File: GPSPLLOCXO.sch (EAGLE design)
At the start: 26 parts, among them IC1 74AC14D, IC2 74LS86D, IC3 74LS390D, IC4 74LS390D, X1 5566-10

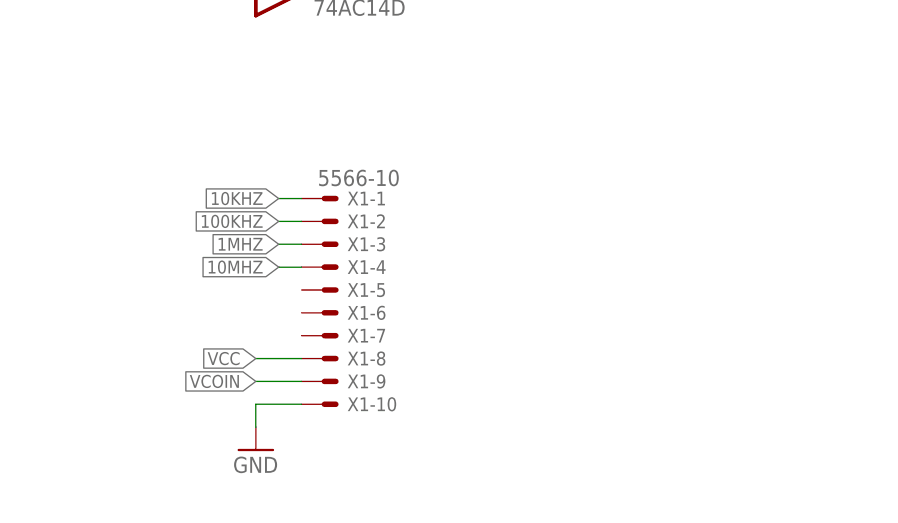
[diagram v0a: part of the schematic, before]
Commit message: Modified board to suite CNC/Milling
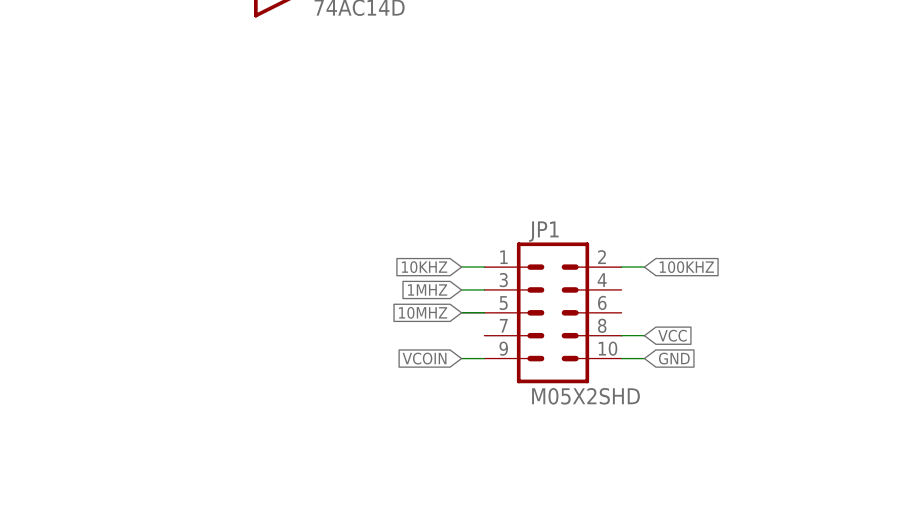
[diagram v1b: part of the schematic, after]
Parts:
- removed X1: 5566-10, con-molex:5566-10
- added JP1: M05X2SHD, SparkFun-Connectors:M05X2SHD
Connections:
- net 100KHZ: now also JP1.2; no longer X1-2.S
- net 10KHZ: now also JP1.1; no longer X1-1.S
- net 10MHZ: now also JP1.5; no longer X1-4.S
- net 1MHZ: now also JP1.3; no longer X1-3.S
- net GND: now also JP1.10; no longer X1-10.S
- net VCC: now also JP1.8; no longer X1-8.S
- net VCOIN: now also JP1.9; no longer X1-9.S
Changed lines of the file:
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@@
 <layer number="54" name="bGND_GNDA" color="1" fill="9" visible="no" active="no"/>
 <layer number="56" name="wert" color="7" fill="1" visible="no" active="no"/>
+<layer number="57" name="tCAD" color="7" fill="1" visible="no" active="no"/>
 <layer number="91" name="Nets" color="2" fill="1" visible="yes" active="yes"/>
 <layer number="92" name="Busses" color="1" fill="1" visible="yes" active="yes"/>
@@
 <layer number="97" name="Info" color="7" fill="1" visible="yes" active="yes"/>
 <layer number="98" name="Guide" color="6" fill="1" visible="yes" active="yes"/>
+<layer number="99" name="SpiceOrder" color="7" fill="1" visible="yes" active="yes"/>
 <layer number="100" name="Muster" color="7" fill="1" visible="no" active="no"/>
 <layer number="101" name="Patch_Top" color="12" fill="4" visible="yes" active="yes"/>
@@
 <layer number="108" name="tplace-old" color="10" fill="1" visible="yes" active="yes"/>
 <layer number="109" name="ref-old" color="11" fill="1" visible="yes" active="yes"/>
+<layer number="110" name="fp0" color="7" fill="1" visible="yes" active="yes"/>
+<layer number="111" name="LPC17xx" color="7" fill="1" visible="yes" active="yes"/>
+<layer number="112" name="tSilk" color="7" fill="1" visible="yes" active="yes"/>
+<layer number="113" name="IDFDebug" color="4" fill="1" visible="yes" active="yes"/>
 <layer number="116" name="Patch_BOT" color="9" fill="4" visible="yes" active="yes"/>
 <layer number="121" name="_tsilk" color="7" fill="1" visible="yes" active="yes"/>
 <layer number="122" name="_bsilk" color="7" fill="1" visible="yes" active="yes"/>
+<layer number="123" name="tTestmark" color="7" fill="1" visible="yes" active="yes"/>
+<layer number="124" name="bTestmark" color="7" fill="1" visible="yes" active="yes"/>
 <layer number="125" name="_tNames" color="7" fill="1" visible="yes" active="yes"/>
+<layer number="126" name="_bNames" color="7" fill="1" visible="yes" active="yes"/>
+<layer number="127" name="_tValues" color="7" fill="1" visible="yes" active="yes"/>
+<layer number="128" name="_bValues" color="7" fill="1" visible="yes" active="yes"/>
+<layer number="131" name="tAdjust" color="7" fill="1" visible="yes" active="yes"/>
+<layer number="132" name="bAdjust" color="7" fill="1" visible="yes" active="yes"/>
 <layer number="144" name="Drill_legend" color="7" fill="1" visible="yes" active="yes"/>
+<layer number="150" name="Notes" color="7" fill="1" visible="yes" active="yes"/>
 <layer number="151" name="HeatSink" color="7" fill="1" visible="yes" active="yes"/>
+<layer number="152" name="_bDocu" color="7" fill="1" visible="yes" active="yes"/>
+<layer number="153" name="FabDoc1" color="7" fill="1" visible="yes" active="yes"/>
+<layer number="154" name="FabDoc2" color="7" fill="1" visible="yes" active="yes"/>
+<layer number="155" name="FabDoc3" color="7" fill="1" visible="yes" active="yes"/>
 <layer number="199" name="Contour" color="7" fill="1" visible="yes" active="yes"/>
 <layer number="200" name="200bmp" color="1" fill="10" visible="yes" active="yes"/>
@@
 <layer number="223" name="223bmp" color="24" fill="1" visible="no" active="no"/>
 <layer number="224" name="224bmp" color="25" fill="1" visible="no" active="no"/>
+<layer number="248" name="Housing" color="7" fill="1" visible="yes" active="yes"/>
+<layer number="249" name="Edge" color="7" fill="1" visible="yes" active="yes"/>
 <layer number="250" name="Descript" color="3" fill="1" visible="no" active="no"/>
 <layer number="251" name="SMDround" color="12" fill="11" visible="no" active="no"/>
@@
 <part name="GND12" library="supply1" deviceset="GND" device=""/>
 <part name="ISOTEMP131-1" library="untitled" deviceset="ISOTEMP-131-191" device=""/>
-<part name="X1" library="con-molex" deviceset="5566-10" device=""/>
-<part name="GND10" library="supply1" deviceset="GND" device=""/>
+<part name="JP1" library="SparkFun-Connectors" deviceset="M05X2" device="SHD"/>
 </parts>
 <sheets>
@@
 <instance part="GND12" gate="1" x="-78.74" y="-17.78"/>
 <instance part="ISOTEMP131-1" gate="ISOTEMP131-191" x="58.42" y="55.88"/>
-<instance part="X1" gate="-1" x="139.7" y="12.7"/>
-<instance part="X1" gate="-2" x="139.7" y="10.16"/>
-<instance part="X1" gate="-3" x="139.7" y="7.62"/>
-<instance part="X1" gate="-4" x="139.7" y="5.08"/>
-<instance part="X1" gate="-5" x="139.7" y="2.54"/>
-<instance part="X1" gate="-6" x="139.7" y="0"/>
-<instance part="X1" gate="-7" x="139.7" y="-2.54"/>
-<instance part="X1" gate="-8" x="139.7" y="-5.08"/>
-<instance part="X1" gate="-9" x="139.7" y="-7.62"/>
-<instance part="X1" gate="-10" x="139.7" y="-10.16"/>
-<instance part="GND10" gate="1" x="132.08" y="-15.24"/>
+<instance part="JP1" gate="G$1" x="165.1" y="0"/>
 </instances>
 <busses>
@@
 </segment>
 <segment>
-<pinref part="X1" gate="-10" pin="S"/>
-<wire x1="137.16" y1="-10.16" x2="132.08" y2="-10.16" width="0.1524" layer="91"/>
-<wire x1="132.08" y1="-10.16" x2="132.08" y2="-12.7" width="0.1524" layer="91"/>
-<pinref part="GND10" gate="1" pin="GND"/>
+<pinref part="JP1" gate="G$1" pin="10"/>
+<wire x1="172.72" y1="-5.08" x2="175.26" y2="-5.08" width="0.1524" layer="91"/>
+<label x="175.26" y="-5.08" size="1.27" layer="95" xref="yes"/>
 </segment>
 </net>
@@
 </segment>
 <segment>
-<pinref part="X1" gate="-8" pin="S"/>
-<wire x1="137.16" y1="-5.08" x2="132.08" y2="-5.08" width="0.1524" layer="91"/>
-<label x="132.08" y="-5.08" size="1.4224" layer="95" rot="R180" xref="yes"/>
+<pinref part="JP1" gate="G$1" pin="8"/>
+<wire x1="172.72" y1="-2.54" x2="175.26" y2="-2.54" width="0.1524" layer="91"/>
+<label x="175.26" y="-2.54" size="1.27" layer="95" xref="yes"/>
 </segment>
 </net>
@@
 </segment>
 <segment>
-<pinref part="X1" gate="-1" pin="S"/>
-<wire x1="137.16" y1="12.7" x2="134.62" y2="12.7" width="0.1524" layer="91"/>
-<label x="134.62" y="12.7" size="1.4224" layer="95" rot="R180" xref="yes"/>
+<pinref part="JP1" gate="G$1" pin="1"/>
+<wire x1="157.48" y1="5.08" x2="154.94" y2="5.08" width="0.1524" layer="91"/>
+<label x="154.94" y="5.08" size="1.27" layer="95" rot="R180" xref="yes"/>
 </segment>
 </net>
@@
 </segment>
 <segment>
-<pinref part="X1" gate="-3" pin="S"/>
-<wire x1="137.16" y1="7.62" x2="134.62" y2="7.62" width="0.1524" layer="91"/>
-<label x="134.62" y="7.62" size="1.4224" layer="95" rot="R180" xref="yes"/>
+<pinref part="JP1" gate="G$1" pin="3"/>
+<wire x1="157.48" y1="2.54" x2="154.94" y2="2.54" width="0.1524" layer="91"/>
+<label x="154.94" y="2.54" size="1.27" layer="95" rot="R180" xref="yes"/>
 </segment>
 </net>
@@
 </segment>
 <segment>
-<pinref part="X1" gate="-2" pin="S"/>
-<wire x1="137.16" y1="10.16" x2="134.62" y2="10.16" width="0.1524" layer="91"/>
-<label x="134.62" y="10.16" size="1.4224" layer="95" rot="R180" xref="yes"/>
+<pinref part="JP1" gate="G$1" pin="2"/>
+<wire x1="172.72" y1="5.08" x2="175.26" y2="5.08" width="0.1524" layer="91"/>
+<label x="175.26" y="5.08" size="1.27" layer="95" xref="yes"/>
 </segment>
 </net>
@@
 </segment>
 <segment>
-<pinref part="X1" gate="-4" pin="S"/>
-<wire x1="137.16" y1="5.08" x2="134.62" y2="5.08" width="0.1524" layer="91"/>
-<label x="134.62" y="5.08" size="1.4224" layer="95" rot="R180" xref="yes"/>
+<pinref part="JP1" gate="G$1" pin="5"/>
+<wire x1="157.48" y1="0" x2="154.94" y2="0" width="0.1524" layer="91"/>
+<label x="154.94" y="0" size="1.27" layer="95" rot="R180" xref="yes"/>
 </segment>
 </net>
@@
 </segment>
 <segment>
-<pinref part="X1" gate="-9" pin="S"/>
-<wire x1="137.16" y1="-7.62" x2="132.08" y2="-7.62" width="0.1524" layer="91"/>
-<label x="132.08" y="-7.62" size="1.4224" layer="95" rot="R180" xref="yes"/>
-</segment>
-</net>
+<pinref part="JP1" gate="G$1" pin="9"/>
+<wire x1="157.48" y1="-5.08" x2="154.94" y2="-5.08" width="0.1524" layer="91"/>
+<label x="154.94" y="-5.08" size="1.27" layer="95" rot="R180" xref="yes"/>
+</segment>
+</net>

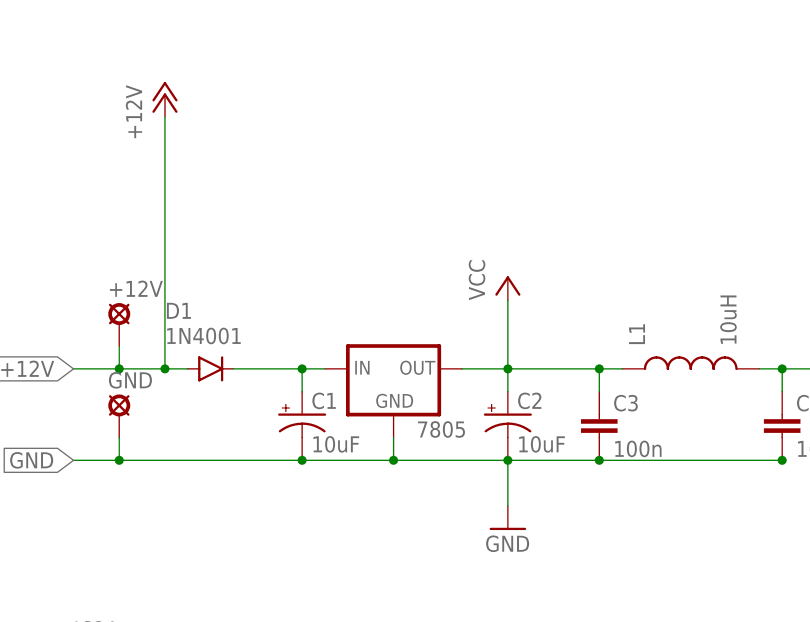
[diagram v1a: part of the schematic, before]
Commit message: Corrected FTDI mapping, added header to select power source.
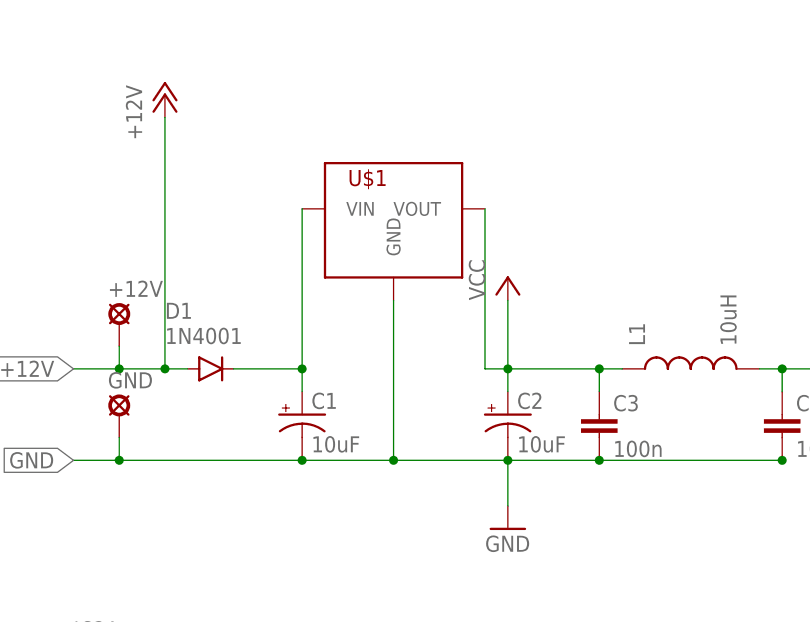
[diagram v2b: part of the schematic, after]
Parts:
- removed 7805: (no value), SparkFun-PowerIC:V_REG_78XXSINK
- added U$1: R-78HBXX-0.5R-78XX-0.5-SIP3, recom:R-78HBXX-0.5R-78XX-0.5-SIP3
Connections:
- net GND: now also U$1.GND; no longer 7805.GND
- net N$1: now also U$1.VIN; no longer 7805.IN
- net VCC: now also U$1.VOUT; no longer 7805.OUT
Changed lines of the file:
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@@
 </classes>
 <parts>
-<part name="7805" library="SparkFun-PowerIC" deviceset="V_REG_78XX" device="SINK"/>
 <part name="D1" library="SparkFun-DiscreteSemi" deviceset="DIODE" device="SMA" value="1N4001"/>
 <part name="C1" library="SparkFun-Capacitors" deviceset="10UF-16V-10%(TANT)" device="" value="10uF"/>
@@
 <part name="ISOTEMP131-1" library="untitled" deviceset="ISOTEMP-131-191" device=""/>
 <part name="JP1" library="SparkFun-Connectors" deviceset="M05X2" device="SHD"/>
+<part name="U$1" library="recom" deviceset="R-78HBXX-0.5" device="R-78XX-0.5-SIP3"/>
 </parts>
 <sheets>
@@
 </plain>
 <instances>
-<instance part="7805" gate="G$1" x="5.08" y="91.44"/>
 <instance part="D1" gate="G$1" x="-15.24" y="91.44" smashed="yes">
 <attribute name="NAME" x="-20.32" y="97.0026" size="1.778" layer="95"/>
@@
 <instance part="ISOTEMP131-1" gate="ISOTEMP131-191" x="58.42" y="55.88"/>
 <instance part="JP1" gate="G$1" x="165.1" y="0"/>
+<instance part="U$1" gate="G$1" x="5.08" y="106.68"/>
 </instances>
 <busses>
@@
 <wire x1="-5.08" y1="81.28" x2="5.08" y2="81.28" width="0.1524" layer="91"/>
 <wire x1="5.08" y1="81.28" x2="17.78" y2="81.28" width="0.1524" layer="91"/>
-<pinref part="7805" gate="G$1" pin="GND"/>
-<wire x1="5.08" y1="81.28" x2="5.08" y2="83.82" width="0.1524" layer="91"/>
 <label x="-30.48" y="81.28" size="1.778" layer="95" rot="R180" xref="yes"/>
 <pinref part="C1" gate="G$1" pin="-"/>
@@
 <pinref part="GND" gate="1" pin="MP"/>
 <wire x1="-25.4" y1="81.28" x2="-25.4" y2="83.82" width="0.1524" layer="91"/>
+<pinref part="U$1" gate="G$1" pin="GND"/>
+<wire x1="5.08" y1="81.28" x2="5.08" y2="99.06" width="0.1524" layer="91"/>
 </segment>
 <segment>
@@
 <net name="VCC" class="0">
 <segment>
-<pinref part="7805" gate="G$1" pin="OUT"/>
-<wire x1="12.7" y1="91.44" x2="17.78" y2="91.44" width="0.1524" layer="91"/>
 <pinref part="C2" gate="G$1" pin="+"/>
 <wire x1="17.78" y1="88.9" x2="17.78" y2="91.44" width="0.1524" layer="91"/>
@@
 <junction x="27.94" y="91.44"/>
 <pinref part="L1" gate="G$1" pin="1"/>
+<wire x1="17.78" y1="91.44" x2="15.24" y2="91.44" width="0.1524" layer="91"/>
+<pinref part="U$1" gate="G$1" pin="VOUT"/>
+<wire x1="15.24" y1="91.44" x2="15.24" y2="109.22" width="0.1524" layer="91"/>
 </segment>
 <segment>
@@
 <segment>
 <pinref part="D1" gate="G$1" pin="C"/>
-<pinref part="7805" gate="G$1" pin="IN"/>
 <wire x1="-12.7" y1="91.44" x2="-5.08" y2="91.44" width="0.1524" layer="91"/>
 <pinref part="C1" gate="G$1" pin="+"/>
-<wire x1="-5.08" y1="91.44" x2="-2.54" y2="91.44" width="0.1524" layer="91"/>
 <wire x1="-5.08" y1="88.9" x2="-5.08" y2="91.44" width="0.1524" layer="91"/>
 <junction x="-5.08" y="91.44"/>
-</segment>
-</net>
+<pinref part="U$1" gate="G$1" pin="VIN"/>
+<wire x1="-5.08" y1="91.44" x2="-5.08" y2="109.22" width="0.1524" layer="91"/>
+</segment>
+</net>
